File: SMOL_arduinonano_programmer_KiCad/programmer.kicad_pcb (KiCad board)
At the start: 2 copper layers, 17.8 x 54 mm, 12 parts, among them J2 Conn_01x05

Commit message: FINALLY fixed the anchor points for mounting holes on SMOL and programmers. Added OSHW logo to library, just in case....
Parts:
- moved HOLE6 1.92 mm to (31.8, 14.1)
- moved HOLE5 1.92 mm to (24.1, 14.1)
- renumbered REF** to HOLE1, REF** to HOLE2, REF** to HOLE3, REF** to HOLE4, REF** to HOLE5, REF** to HOLE6
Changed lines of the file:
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@@
-(kicad_pcb (version 20171130) (host pcbnew "(5.0.2)-1")
+(kicad_pcb (version 20171130) (host pcbnew "(5.1.2)-1")
   (general
     (thickness 1.6)
@@
     (zone_45_only no)
     (trace_min 0.2)
-    (segment_width 0.1016)
-    (edge_width 0.1016)
     (via_size 0.6096)
     (via_drill 0.4064)
@@
     (uvia_min_size 0.2)
     (uvia_min_drill 0.1)
+    (edge_width 0.1016)
+    (segment_width 0.1016)
     (pcb_text_width 0.3)
     (pcb_text_size 1.5 1.5)
@@
   )
   (module Wire_Pads:SolderWirePad_single_1mmDrill (layer F.Cu)
-    (at 29.845 14.351 90)
-    (fp_text reference REF** (at 0 -3.81 90) (layer F.SilkS) hide
+    (at 31.75 14.097 90)
+    (fp_text reference HOLE6 (at 0 -3.81 90) (layer F.SilkS) hide
       (effects (font (size 1 1) (thickness 0.15)))
     )
@@
       (effects (font (size 1 1) (thickness 0.15)))
     )
-    (pad 1 thru_hole oval (at 0.254 1.905 90) (size 1.524 1.524) (drill 1 (offset 0.2032 0)) (layers *.Cu *.Mask))
+    (pad 1 thru_hole oval (at 0 0 90) (size 1.524 1.524) (drill 1 (offset 0.2032 0)) (layers *.Cu *.Mask))
   )
   (module Mounting_Holes:MountingHole_3.2mm_M3 (layer F.Cu)
@@
     (tags "mounting hole 3.2mm no annular m3")
     (attr virtual)
-    (fp_text reference REF** (at 0 -4.2) (layer F.SilkS) hide
+    (fp_text reference HOLE2 (at 0 -4.2) (layer F.SilkS) hide
       (effects (font (size 1 1) (thickness 0.15)))
     )
@@
     (tags "mounting hole 3.2mm no annular m3")
     (attr virtual)
-    (fp_text reference REF** (at 0 -4.2) (layer F.SilkS) hide
+    (fp_text reference HOLE4 (at 0 -4.2) (layer F.SilkS) hide
       (effects (font (size 1 1) (thickness 0.15)))
     )
@@
     (tags "mounting hole 3.2mm no annular m3")
     (attr virtual)
-    (fp_text reference REF** (at 0 -4.2) (layer F.SilkS) hide
+    (fp_text reference HOLE3 (at 0 -4.2) (layer F.SilkS) hide
       (effects (font (size 1 1) (thickness 0.15)))
     )
@@
     (tags "mounting hole 3.2mm no annular m3")
     (attr virtual)
-    (fp_text reference REF** (at 0 -4.2) (layer F.SilkS) hide
+    (fp_text reference HOLE1 (at 0 -4.2) (layer F.SilkS) hide
       (effects (font (size 1 1) (thickness 0.15)))
     )
@@
   )
   (module Wire_Pads:SolderWirePad_single_1mmDrill (layer F.Cu)
-    (at 22.225 14.351 90)
-    (fp_text reference REF** (at 0 -3.81 90) (layer F.SilkS) hide
+    (at 24.13 14.097 90)
+    (fp_text reference HOLE5 (at 0 -3.81 90) (layer F.SilkS) hide
       (effects (font (size 1 1) (thickness 0.15)))
     )
@@
       (effects (font (size 1 1) (thickness 0.15)))
     )
-    (pad 1 thru_hole oval (at 0.254 1.905 90) (size 1.524 1.524) (drill 1 (offset 0.2032 0)) (layers *.Cu *.Mask))
+    (pad 1 thru_hole oval (at 0 0 90) (size 1.524 1.524) (drill 1 (offset 0.2032 0)) (layers *.Cu *.Mask))
   )
   (gr_text CLK (at 34.163 59.69) (layer F.SilkS)

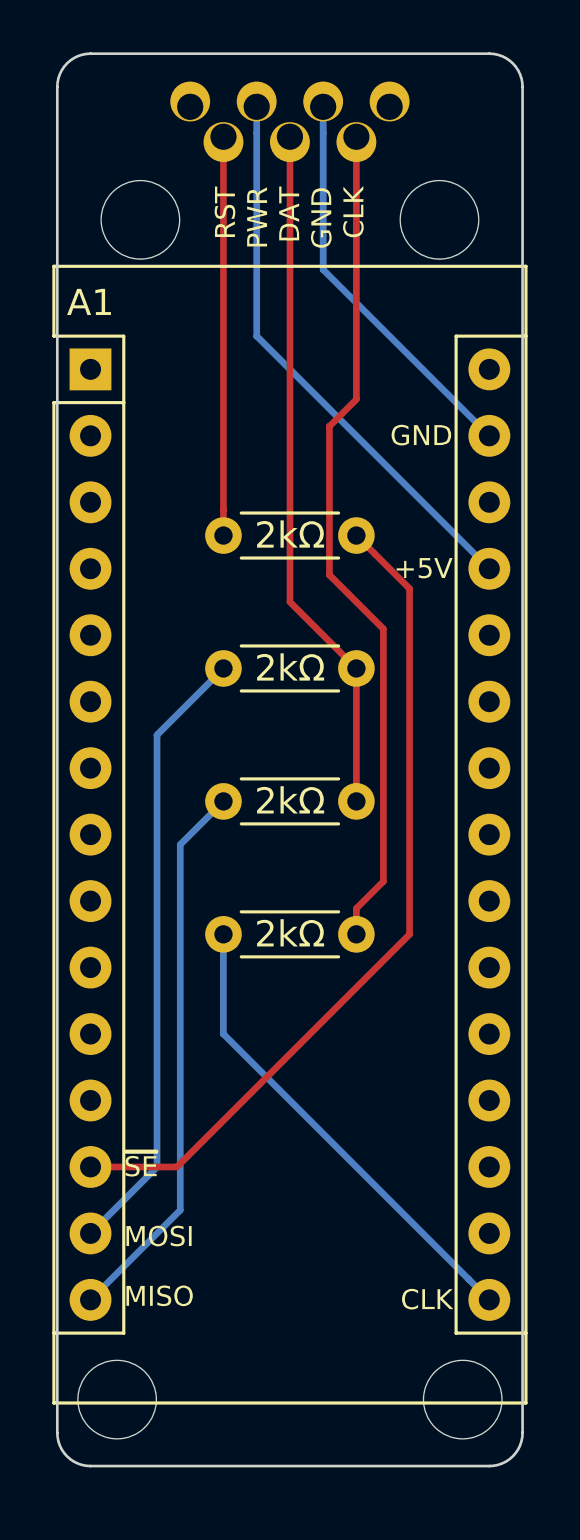
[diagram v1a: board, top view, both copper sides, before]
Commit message: Updated the USBasp programmer; updated programmer silkscreens
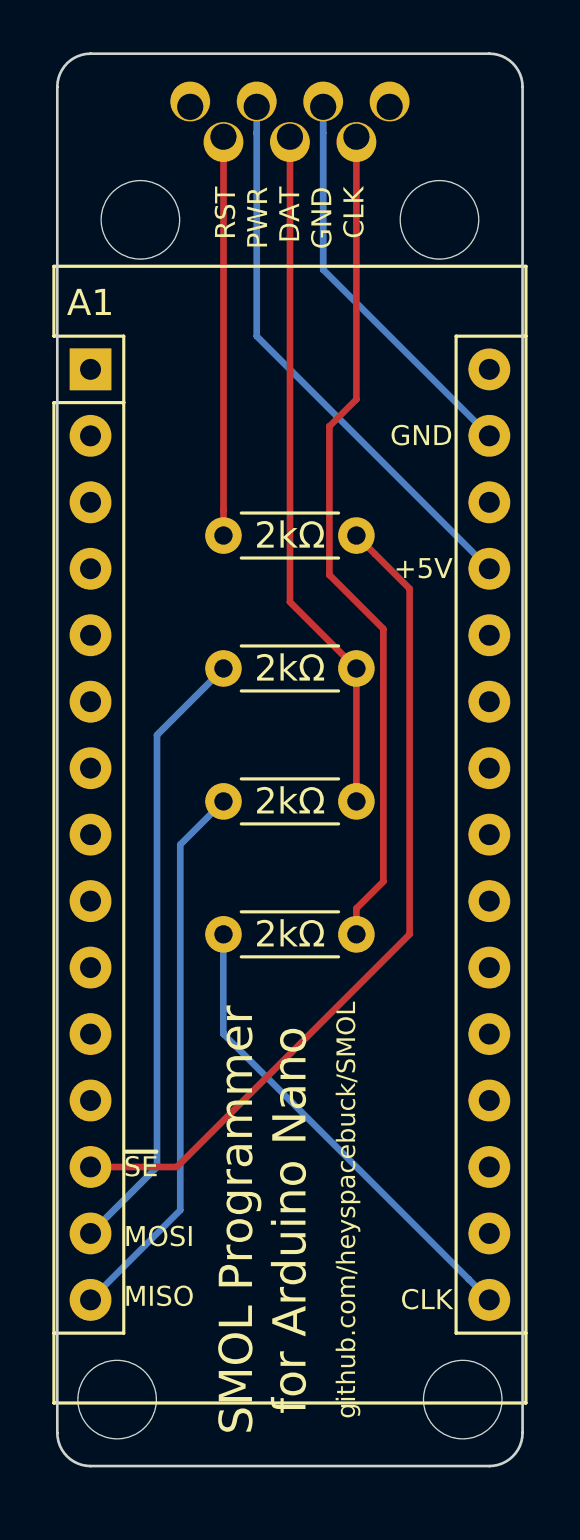
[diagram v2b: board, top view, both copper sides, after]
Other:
- board text added: "SMOL Programmer for Arduino Nano"
- board text added: "github.com/heyspacebuck/SMOL"
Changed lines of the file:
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@@
   (general
     (thickness 1.6)
-    (drawings 15)
+    (drawings 17)
     (tracks 34)
     (zones 0)
@@
     (pad 1 thru_hole oval (at 0 0 90) (size 1.524 1.524) (drill 1 (offset 0.2032 0)) (layers *.Cu *.Mask))
   )
+  (gr_text github.com/heyspacebuck/SMOL (at 30.099 56.261 90) (layer F.SilkS)
+    (effects (font (size 0.7112 0.7112) (thickness 0.1524)))
+  )
+  (gr_text "SMOL Programmer\nfor Arduino Nano" (at 26.924 56.642 90) (layer F.SilkS)
+    (effects (font (size 1.27 1.27) (thickness 0.2032)))
+  )
   (gr_text CLK (at 34.163 59.69) (layer F.SilkS)
